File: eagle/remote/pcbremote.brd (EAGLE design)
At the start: 44.4 x 116.1 mm, 33 parts, among them Q1 FDC638P, U2 ATMEGA328P_TQFP, U3 LTC1540CS8PBF, U4 MCP73831/OT, U5 LTC4412ES6TRPBF, U6 MIC5301-3.3YD5-TR, Y2 8MHz

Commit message: Snapped to grid
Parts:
- removed R2: 2.26Meg, rcl:R0805
- removed R3: 0, rcl:R0805
- removed R4: 1.18Meg, rcl:R0805
- added HALL, TRIGGER: JST-XH-02-PIN-ROUND-PAD, Rembrandt Electronics - JST XH Connectors v1-0:JST-XH-02-PACKAGE-ROUND-PAD
- added MASTER_SW, UART: 455-1750-1-ND, SparkFun-Connectors:1X03
- added R10, R11: 10k, rcl:R0805
- added VR1: 3296W-1-502, 3296W-1-502:TRIM_3296W-1-502
- moved OLED_CONN 32.9 mm to (-25.4, 24.1), turned to 270 degrees
- moved C2 25.3 mm to (-24.1, 7.62), turned to 0 degrees
- moved R7 22.6 mm to (-24.1, 10.2), turned to 0 degrees
- moved C6 20.8 mm to (-24.1, 12.7), turned to 0 degrees
- moved R8 20.0 mm to (-24.1, 15.2), turned to 0 degrees
- moved C5 18.7 mm to (-44.5, 7.62), turned to 270 degrees
- moved Y2 17.6 mm to (-40.6, 8.89), turned to 270 degrees
- moved C4 16.8 mm to (-44.5, 12.7)
- moved C3 15.4 mm to (-40.6, 13.7), turned to 180 degrees
- moved PROG_CONN 11.2 mm to (-39.4, -3.81), turned to 180 degrees
- moved R1 8.99 mm to (-44.5, 17.8), turned to 90 degrees
- moved USB_IN 7.79 mm to (-27.9, -22.9)
- moved U2 7.21 mm to (-32.6, 12.7), turned to 359.8 degrees
- moved U3 6.50 mm to (-25.9, -7.45), turned to 0 degrees
- moved C9 2.94 mm to (-33.0, 2.54)
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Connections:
- removed net N$2: R2.1, R3.1
- new net N$10: CONN_BAT.2, MASTER_SW.2
- net A2: now also R10.1, R11.2
- net A3: now also HALL.2
- net D0: now also UART.2
- net D1: now also UART.3
- net D2: now also TRIGGER.2
- net GND: now also HALL.1, R11.1, TRIGGER.1, UART.1, VR1.3; no longer R4.1
- net N$1: now also VR1.2; no longer R2.2, R4.2
- net VIN: now also VR1.1; no longer R3.2
- net V_BATT: now also MASTER_SW.1, R10.2; no longer CONN_BAT.2
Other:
- board size 44.4 x 116.1 mm -> 50.7 x 111 mm
- board text removed: "-"

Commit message: Pre-airwire, everything labeled
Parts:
- removed C20: 1u, rcl:C0805
- removed HALL, TRIGGER: JST-XH-02-PIN-ROUND-PAD, Rembrandt Electronics - JST XH Connectors v1-0:JST-XH-02-PACKAGE-ROUND-PAD
- removed OLED_CONN: JST-XH-04-PIN-ROUND-PAD, Rembrandt Electronics - JST XH Connectors v1-0:JST-XH-04-PACKAGE-ROUND-PAD
- removed R10, R11: 10k, rcl:R0805
- removed R9: 470k, rcl:R0805
- removed U5: LTC4412ES6TRPBF, LTC4412:TSOT-23_S6_LIT
- removed U6: MIC5301-3.3YD5-TR, MIC5301:TSOT-23-5_D5_MCH
- removed UART: 455-1750-1-ND, SparkFun-Connectors:1X03
- removed Y2: 8MHz, SparkFun-Clocks:CRYSTAL-SMD-5X3.2-4PAD
- added C10: 4.7u, rcl:C0805
- added IC1: MCP73831/OT, adafruit:SOT23-5L
- added J6: 455-1750-1-ND, SparkFun-Connectors:1X03
- added R2: 10k, rcl:R0805
- added R3: 470, rcl:R0805
- added R4: 2k, rcl:R0805
- added U1: LTC1540CS8PBF, LTC_1450:SO-8_S_LIT
- added X1: JST-XH-04-PIN-ROUND-PAD, Rembrandt Electronics - JST XH Connectors v1-0:JST-XH-04-PACKAGE-ROUND-PAD
- added X3, X4, X5, X6: JST-XH-02-PIN-ROUND-PAD, Rembrandt Electronics - JST XH Connectors v1-0:JST-XH-02-PACKAGE-ROUND-PAD
- added Y1: 8MHz, SparkFun-Clocks:CRYSTAL-SMD-5X3.2-4PAD
- C1: value 0.01u -> 1u
- C2: value .1u -> 0.01u
- C3: value .1u -> 1u
- C4, C5: value 22p -> .1u
- C6: value .1u -> 22p
- C7: value 4.7u -> 22p
- C8: value 4.7u -> .1u
- C9: value 1u -> 4.7u
- R1: value 10k -> 470k
- R5: value 2k -> 10k
- R6: value 470 -> 10k
- U2: value ATMEGA328P_TQFP -> LTC4412ES6TRPBF; device SparkFun-IC-Microcontroller:TQFP32-08 -> LTC4412:TSOT-23_S6_LIT
- U3: value LTC1540CS8PBF -> MIC5301-3.3YD5-TR; device LTC_1450:SO-8_S_LIT -> MIC5301:TSOT-23-5_D5_MCH
- U4: value MCP73831/OT -> ATMEGA328P_TQFP; device adafruit:SOT23-5L -> SparkFun-IC-Microcontroller:TQFP32-08
- moved R6 36.6 mm to (-24.1, 15.2), turned to 0 degrees
- moved R1 35.3 mm to (-26.7, -12.7)
- moved C8 33.3 mm to (-24.1, 12.7), turned to 0 degrees
- moved C7 33.1 mm to (-44.5, 8.89), turned to 270 degrees
- moved U4 31.8 mm to (-32.6, 12.7), turned to 359.8 degrees
- moved R5 29.2 mm to (-24.1, 10.2), turned to 0 degrees
- moved U2 26.8 mm to (-30.5, -14.0), turned to 0 degrees
- moved C9 22.5 mm to (-26.7, -19.1), turned to 90 degrees
- moved C3 21.0 mm to (-22.9, 2.54), turned to 270 degrees
- moved C4 20.9 mm to (-24.1, 7.62), turned to 0 degrees
- moved C6 20.4 mm to (-44.5, 14.0), turned to 270 degrees
- moved R7 19.9 mm to (-41.9, 19.1), turned to 90 degrees
- moved R8 15.7 mm to (-39.4, 19.1), turned to 270 degrees
- moved U3 10.5 mm to (-29.2, 2.54)
- moved C5 8.29 mm to (-40.6, 15.0), turned to 180 degrees
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- renumbered CONN_BAT to CN1, LED_EXT to X2, MASTER_SW to J2, NRF_CONN to J4, PROG_CONN to J5, USB_IN to J1
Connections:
- net 3.3V: now also C4.1, C5.1, R2.1, R5.2, R6.2, U3.5, U4.18, U4.4, U4.6, X1.2; no longer C2.1, C20.1, OLED_CONN.2, R1.1, R7.2, R8.2, U2.18, U2.4, U2.6, U6.5
- net A0: now also U4.23; no longer U2.23
- net A1: now also U4.24; no longer U2.24
- net A2: now also R7.1, R8.2, U4.25; no longer R10.1, R11.2, U2.25
- net A3: now also U4.26, X4.2; no longer HALL.2, U2.26
- net AREF: now also C8.1, U4.20; no longer C6.1, U2.20
- net CE: now also U4.13; no longer U2.13
- net CSN: now also U4.14; no longer U2.14
- net D0: now also J6.2, U4.30; no longer U2.30, UART.2
- net D1: now also J6.3, U4.31; no longer U2.31, UART.3
- net D2: now also U4.32, X3.2; no longer TRIGGER.2, U2.32
- net D3: now also U4.1, X5.2; no longer U2.1
- net D4: now also U4.2, X6.2; no longer U2.2
- net D5: now also U4.9; no longer U2.9
- net D6: now also U4.10; no longer U2.10
- net D7: now also U4.11; no longer U2.11
- net D8: now also U4.12; no longer U2.12
- net GND: now also C10.2, IC1.2, J6.1, R4.2, R8.1, U1.1, U1.2, U2.2, U4.21, U4.3, U4.5, X1.1, X3.1, X4.1, X5.1, X6.1; no longer C20.2, HALL.1, OLED_CONN.1, R11.1, R5.2, TRIGGER.1, U2.21, U2.5, U3.1, U4.2, U5.2, U5.3, U6.2, UART.1
- net MISO: now also U4.16; no longer U2.16
- net MOSI: now also U4.15; no longer U2.15
- net N$1: now also U1.3; no longer U3.3
- net N$13: now also R1.1, U2.4; no longer R9.1, U5.4
- net N$3: now also IC1.5, R4.1; no longer R5.1, U4.5
- net N$4: now also IC1.1, R3.1; no longer R6.1, U4.1
- net N$5: now also R3.2; no longer R6.2
- net N$6: now also R5.1, U4.19; no longer R7.1, U2.19
- net N$7: now also R6.1, U4.22; no longer R8.1, U2.22
- net N$8: now also C2.1, U3.4; no longer C1.1, U6.4
- net N$9: now also U2.5; no longer U5.5
- net REF: now also U1.4, U1.5, U1.6; no longer U3.4, U3.5, U3.6
- net RST: now also R2.2, U4.29; no longer R1.2, U2.29
- net SCK: now also U4.17; no longer U2.17
- net SCL: now also U4.28, X1.3; no longer OLED_CONN.3, U2.28
- net SDA: now also U4.27, X1.4; no longer OLED_CONN.4, U2.27
- net STATUS: now also U1.8, U3.3; no longer U3.8, U6.3
- net VIN: now also C1.1, R1.2, U1.7, U2.6, U3.1; no longer C9.1, R9.2, U3.7, U5.6, U6.1
- net V_BATT: now also C10.1, IC1.3, R7.2, U2.1; no longer C8.1, R10.2, U4.3, U5.1
- net V_USB: now also C9.1, IC1.4; no longer C7.1, U4.4
- net XTAL1: now also C6.1, U4.7, Y1.1; no longer C4.1, U2.7, Y2.1
- net XTAL2: now also C7.1, U4.8, Y1.3; no longer C5.1, U2.8, Y2.3
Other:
- board text added: "-"
- board text added: "BATT"
- board text added: "CHRG LED"
- board text added: "DEADMAN"
- board text added: "HALL"
- board text added: "LED"
- board text added: "MAIN SWITCH"
- board text added: "MP BUTTON"
- board text added: "NRF"
- board text added: "OLED"
- board text added: "PROG"
- board text added: "RX"
- board text added: "TX"
- board text added: "UART"
- board text added: "USB PWR"
- board text removed: "+"

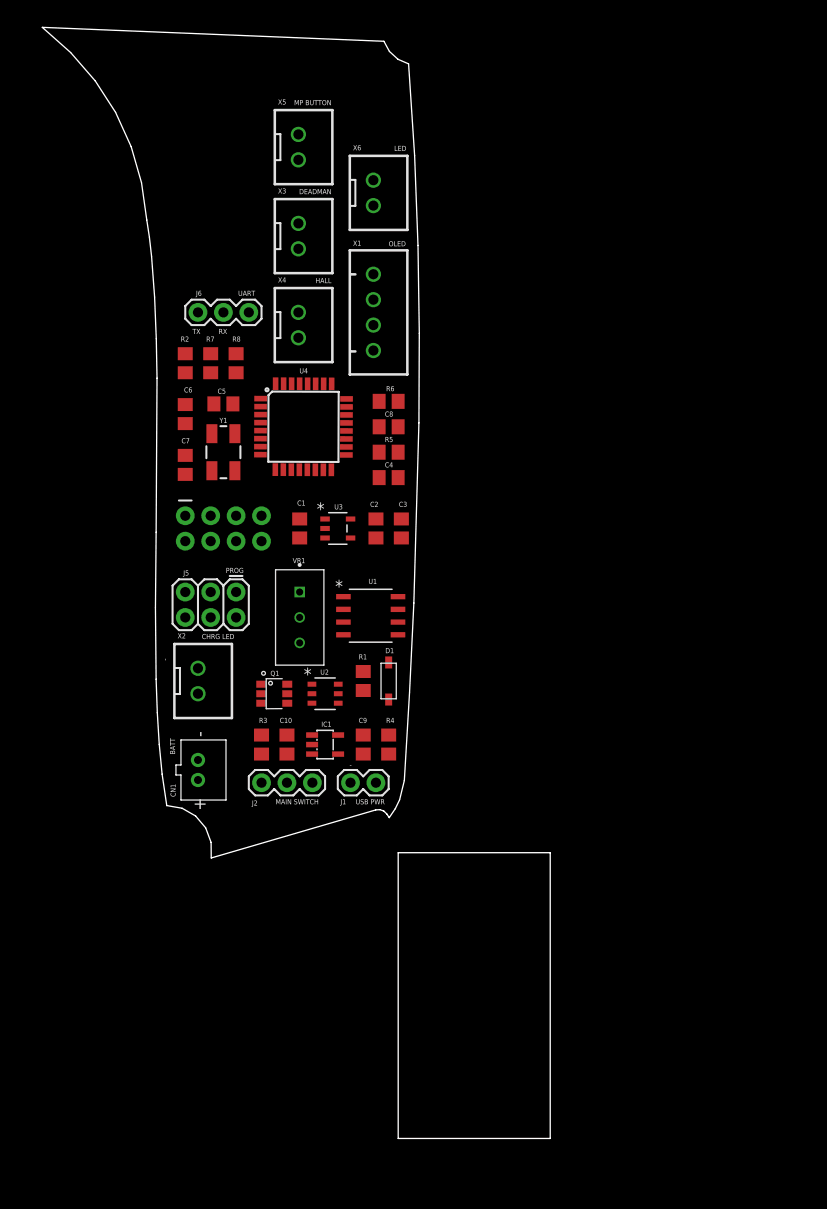
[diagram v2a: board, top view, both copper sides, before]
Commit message: Airwire no gnd
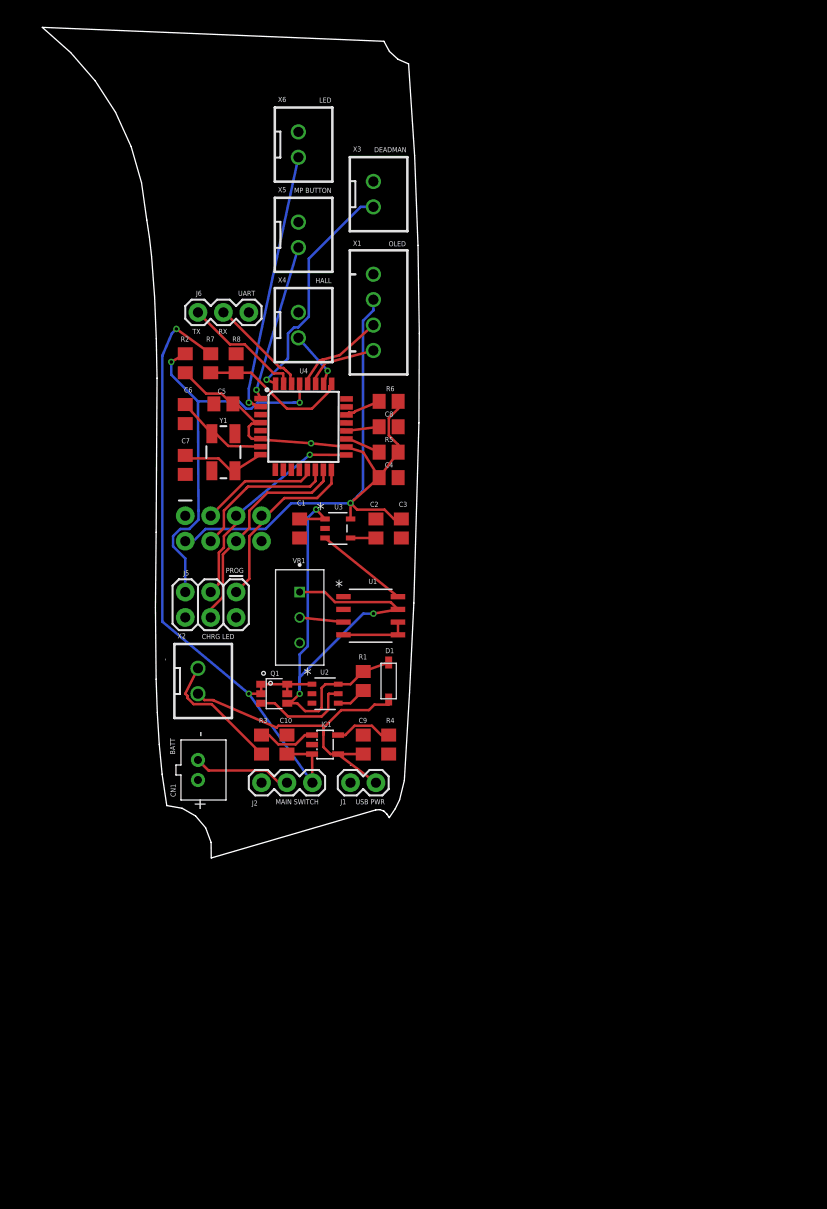
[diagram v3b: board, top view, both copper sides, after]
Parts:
- moved X6 8.91 mm to (-33.1, 40.9)
- moved X5 8.76 mm to (-33.1, 31.9)
- moved X3 8.59 mm to (-25.7, 35.9)
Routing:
- net 3.3V: track 0.00 -> 86.1 mm, vias 0 -> 2
- net V_BATT: track 0.00 -> 69.6 mm, vias 0 -> 2
- net VIN: track 0.00 -> 62.7 mm, vias 0 -> 3
- net RST: track 0.00 -> 41.0 mm, vias 0 -> 2
- net V_USB: track 0.00 -> 33.3 mm
- net D4: track 0.00 -> 26.3 mm, vias 0 -> 1
- net D2: track 0.00 -> 23.7 mm, vias 0 -> 1
- net MOSI: track 0.00 -> 22.0 mm
- net SCK: track 0.00 -> 21.9 mm, vias 0 -> 1
- net MISO: track 0.00 -> 18.4 mm
- net D3: track 0.00 -> 15.8 mm, vias 0 -> 1
- net CSN: track 0.00 -> 15.2 mm
- net A2: track 0.00 -> 14.9 mm
- net N$5: track 0.00 -> 13.1 mm
- net D1: track 0.00 -> 12.1 mm
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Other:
- board size 50.7 x 111 mm -> 37.7 x 83 mm

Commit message: Added mounting holes and routing spots
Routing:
- net GND: track 0.00 -> 9.45 mm, vias 0 -> 4
- added copper zone on layer 1, net GND
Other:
- outline, holes or cut-outs redrawn
